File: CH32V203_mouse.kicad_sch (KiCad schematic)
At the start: 18 parts, among them J1 USB_C_Receptacle_USB2.0_16P_u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, U1 CH32V203G6U6, U2 USBLC6-2SC6, U3 XC6206P332MR, X1 16MHz

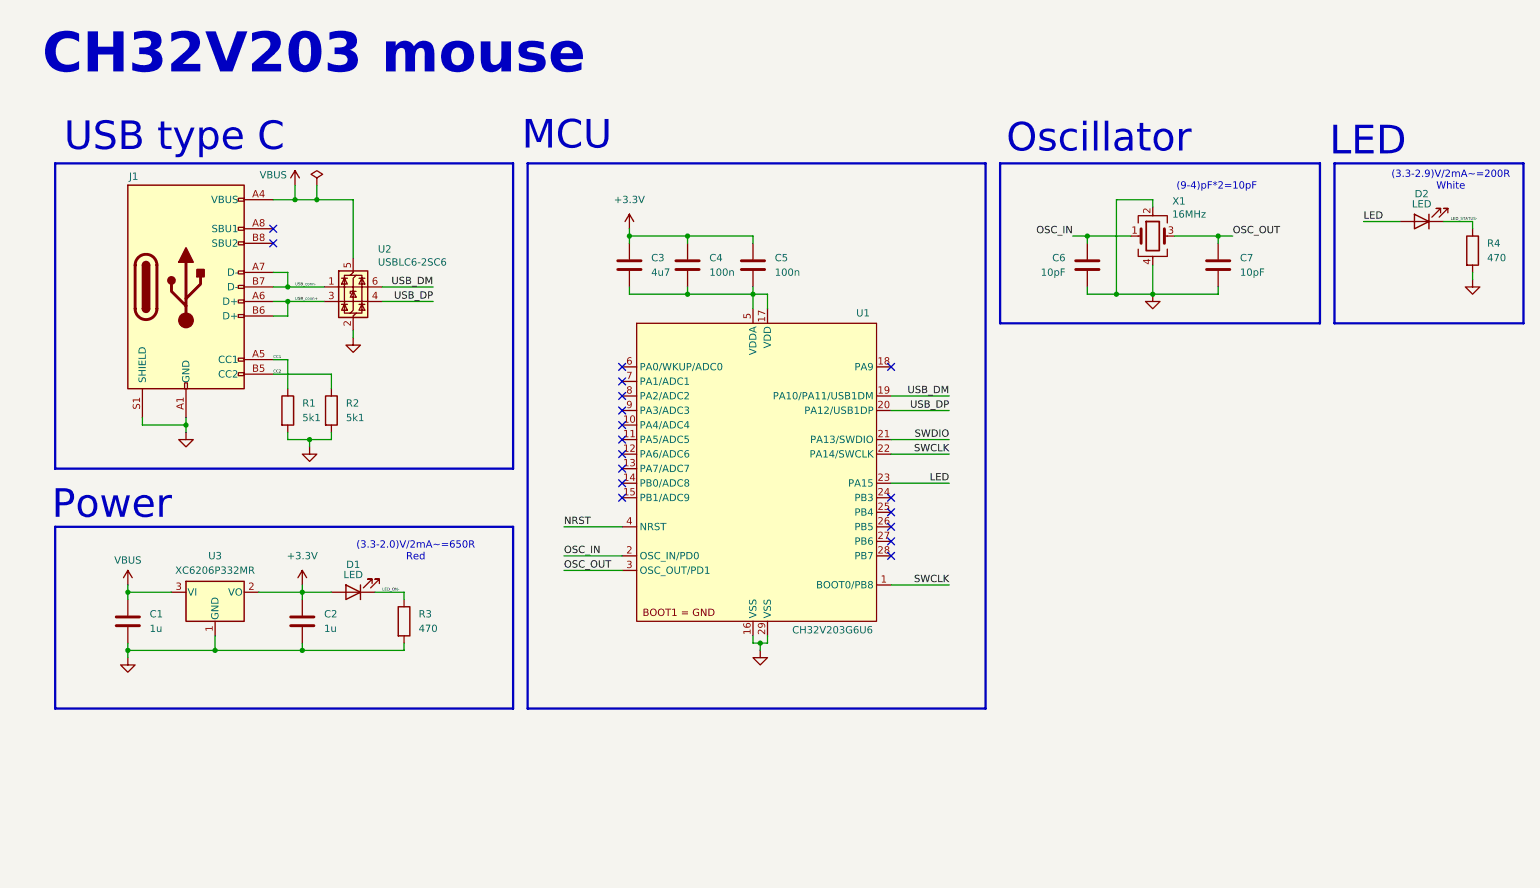
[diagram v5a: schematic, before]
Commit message: Switch circuit reset circuit debugging and UART connectors mounting holes
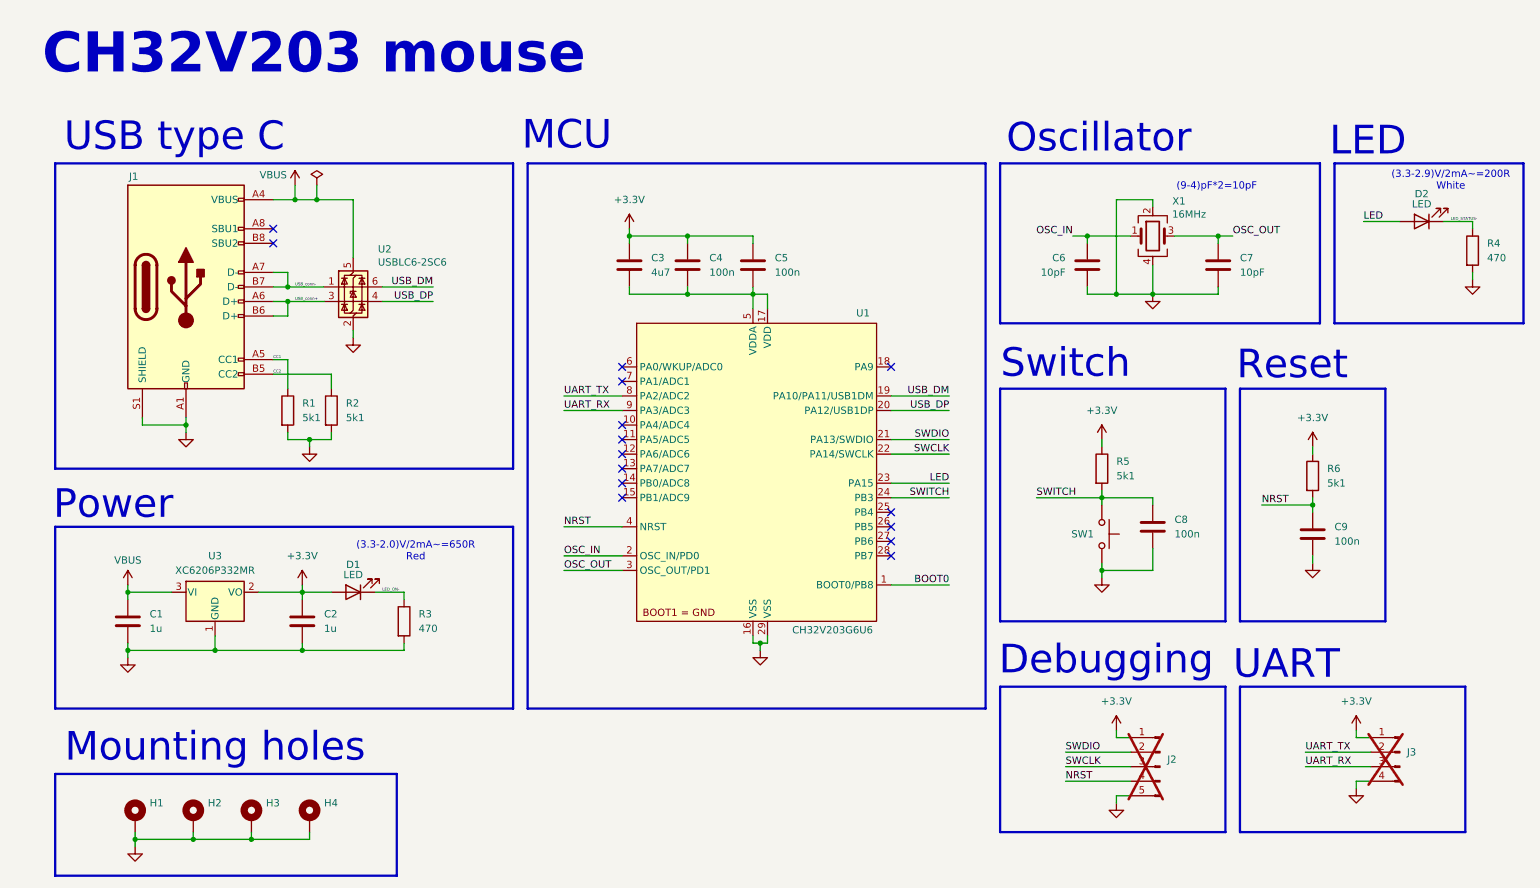
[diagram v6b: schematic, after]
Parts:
- added C8, C9: 100n, symbol Device:C
- added H1, H2, H3, H4: MountingHole_Pad, symbol Mechanical:MountingHole_Pad
- added J2: Conn_01x05_Pin, symbol Connector:Conn_01x05_Pin
- added J3: Conn_01x04_Pin, symbol Connector:Conn_01x04_Pin
- added R5, R6: 5k1, symbol Device:R
- added SW1: SW_Push, symbol Switch:SW_Push
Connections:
- net +3.3V: now also J2.1 (Pin_1), J3.1 (Pin_1), R5.1, R6.1
- net GND: now also C8.2, C9.2, H1.1, H2.1, H3.1, H4.1, J2.5 (Pin_5), J3.4 (Pin_4), SW1.2
- net NRST: now also C9.1, J2.4 (Pin_4), R6.2
- net SWCLK: now also J2.3 (Pin_3); no longer U1.1 (BOOT0/PB8)
- net SWDIO: now also J2.2 (Pin_2)
- net SWITCH: now reaches U1.24 (PB3)
- net SWITCH: now also C8.1, R5.2, SW1.1
- net UART_TX: now reaches U1.8 (PA2/ADC2)
- net UART_TX: now also J3.2 (Pin_2)
- net UART_RX: now reaches U1.9 (PA3/ADC3)
- net UART_RX: now also J3.3 (Pin_3)
- new net BOOT0: U1.1 (BOOT0/PB8)
- no-connect marks 18 -> 15
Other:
- note added: "Debugging"
- note added: "Mounting holes"
- note added: "Reset"
- note added: "Switch"
- note added: "UART"

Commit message: BOOT0 pull-down missing power flags
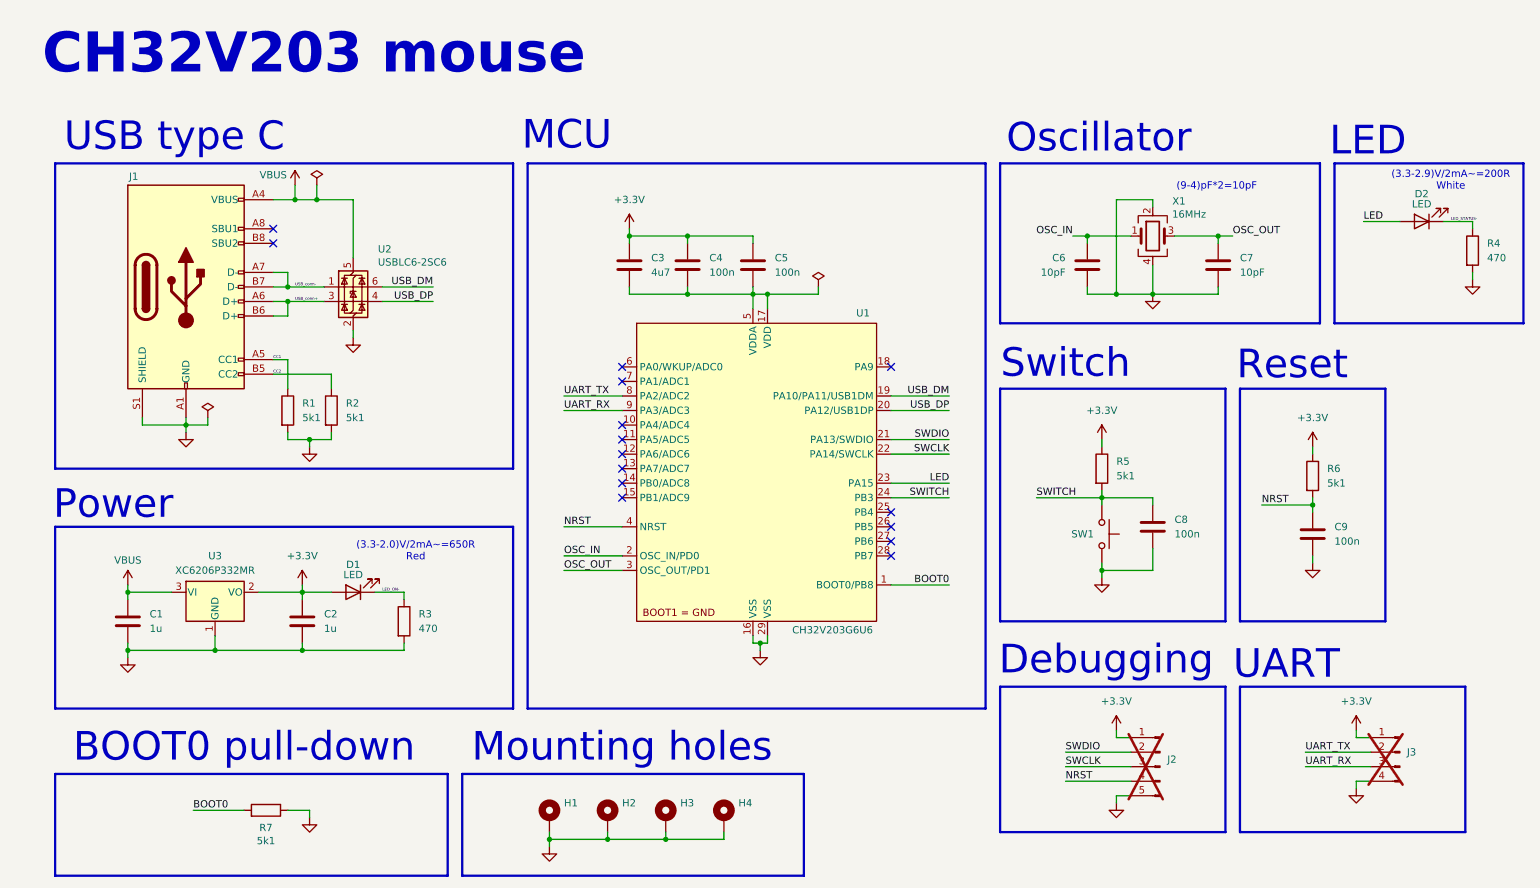
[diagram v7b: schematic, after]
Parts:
- added R7: 5k1, symbol Device:R
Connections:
- net BOOT0: now also R7.2
- net GND: now also R7.1
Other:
- note added: "BOOT0 pull-down"
- moved on the sheet: H1, H2, H3, H4

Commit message: Footprints selected
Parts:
- C1, C2, C3: footprint (none) -> Capacitor_SMD:C_0603_1608Metric_Pad1.08x0.95mm_HandSolder
- C4, C5, C6, C7, C8, C9, D1, D2: footprint (none) -> Capacitor_SMD:C_0402_1005Metric
- H1, H2, H3, H4: footprint (none) -> MountingHole:MountingHole_3.2mm_M3_DIN965_Pad
- J1: footprint (none) -> Connector_USB:USB_C_Receptacle_Palconn_UTC16-G
- J2: footprint (none) -> Connector_PinHeader_2.54mm:PinHeader_1x05_P2.54mm_Vertical
- J3: footprint (none) -> Connector_PinHeader_2.54mm:PinHeader_1x04_P2.54mm_Vertical
- R1, R2, R3, R4, R5, R6, R7: footprint (none) -> Resistor_SMD:R_0402_1005Metric
- SW1: footprint (none) -> Button_Switch_THT:SW_PUSH_6mm_H4.3mm
- X1: footprint (none) -> Crystal:Crystal_SMD_3225-4Pin_3.2x2.5mm
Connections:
- net VDD: now reaches C3.2, C4.2, C5.2, U1.17 (VDD), U1.5 (VDDA)
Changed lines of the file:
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@@
 		)
 	)
+	(label "VDD"
+		(at 146.05 64.77 0)
+		(fields_autoplaced yes)
+		(effects
+			(font
+				(size 0.5 0.5)
+			)
+			(justify left bottom)
+		)
+	)
 	(label "SWITCH"
 		(at 191.77 100.33 0)
@@
 			)
 		)
-		(property "Footprint" ""
+		(property "Footprint" "Resistor_SMD:R_0402_1005Metric"
 			(at 57.15 156.718 90)
 			(effects
@@
 			)
 		)
-		(property "Footprint" ""
+		(property "Footprint" "Capacitor_SMD:C_0402_1005Metric"
 			(at 131.7752 63.5 0)
 			(effects
@@
 			)
 		)
-		(property "Footprint" ""
+		(property "Footprint" "Capacitor_SMD:C_0402_1005Metric"
 			(at 72.39 116.84 0)
 			(effects
@@
 			)
 		)
-		(property "Footprint" ""
+		(property "Footprint" "Connector_PinHeader_2.54mm:PinHeader_1x04_P2.54mm_Vertical"
 			(at 255.27 144.78 0)
 			(effects
@@
 			)
 		)
-		(property "Footprint" ""
+		(property "Footprint" "Capacitor_SMD:C_0603_1608Metric_Pad1.08x0.95mm_HandSolder"
 			(at 64.4652 125.73 0)
 			(effects
@@
 			)
 		)
-		(property "Footprint" ""
+		(property "Footprint" "MountingHole:MountingHole_3.2mm_M3_DIN965_Pad"
 			(at 127 156.21 0)
 			(effects
@@
 			)
 		)
-		(property "Footprint" ""
+		(property "Footprint" "Resistor_SMD:R_0402_1005Metric"
 			(at 59.182 85.09 90)
 			(effects
@@
 			)
 		)
-		(property "Footprint" ""
+		(property "Footprint" "Capacitor_SMD:C_0603_1608Metric_Pad1.08x0.95mm_HandSolder"
 			(at 33.9852 125.73 0)
 			(effects
@@
 			)
 		)
-		(property "Footprint" ""
+		(property "Footprint" "MountingHole:MountingHole_3.2mm_M3_DIN965_Pad"
 			(at 137.16 156.21 0)
 			(effects
@@
 			)
 		)
-		(property "Footprint" ""
+		(property "Footprint" "Crystal:Crystal_SMD_3225-4Pin_3.2x2.5mm"
 			(at 212.09 54.61 0)
 			(effects
@@
 			)
 		)
-		(property "Footprint" ""
+		(property "Footprint" "Resistor_SMD:R_0402_1005Metric"
 			(at 266.192 57.15 90)
 			(effects
@@
 			)
 		)
-		(property "Footprint" ""
+		(property "Footprint" "Capacitor_SMD:C_0402_1005Metric"
 			(at 213.0552 109.22 0)
 			(effects
@@
 			)
 		)
-		(property "Footprint" ""
+		(property "Footprint" "Capacitor_SMD:C_0402_1005Metric"
 			(at 199.6948 63.5 0)
 			(effects
@@
 			)
 		)
-		(property "Footprint" ""
+		(property "Footprint" "Capacitor_SMD:C_0402_1005Metric"
 			(at 224.4852 63.5 0)
 			(effects
@@
 			)
 		)
-		(property "Footprint" ""
+		(property "Footprint" "Resistor_SMD:R_0402_1005Metric"
 			(at 66.802 85.09 90)
 			(effects
@@
 			)
 		)
-		(property "Footprint" ""
+		(property "Footprint" "Connector_PinHeader_2.54mm:PinHeader_1x05_P2.54mm_Vertical"
 			(at 213.36 147.32 0)
 			(effects
@@
 			)
 		)
-		(property "Footprint" ""
+		(property "Footprint" "Resistor_SMD:R_0402_1005Metric"
 			(at 238.252 96.52 90)
 			(effects
@@
 			)
 		)
-		(property "Footprint" ""
+		(property "Footprint" "Capacitor_SMD:C_0603_1608Metric_Pad1.08x0.95mm_HandSolder"
 			(at 121.6152 63.5 0)
 			(effects
@@
 			)
 		)
-		(property "Footprint" ""
+		(property "Footprint" "Resistor_SMD:R_0402_1005Metric"
 			(at 79.502 121.92 90)
 			(effects
@@
 			)
 		)
-		(property "Footprint" ""
+		(property "Footprint" "Resistor_SMD:R_0402_1005Metric"
 			(at 201.422 95.25 90)
 			(effects
@@
 			)
 		)
-		(property "Footprint" ""
+		(property "Footprint" "Button_Switch_THT:SW_PUSH_6mm_H4.3mm"
 			(at 208.28 106.68 0)
 			(effects
@@
 			)
 		)
-		(property "Footprint" ""
+		(property "Footprint" "MountingHole:MountingHole_3.2mm_M3_DIN965_Pad"
 			(at 106.68 156.21 0)
 			(effects
@@
 			)
 		)
-		(property "Footprint" ""
+		(property "Footprint" "Capacitor_SMD:C_0402_1005Metric"
 			(at 259.08 52.07 0)
 			(effects
@@
 			)
 		)
-		(property "Footprint" ""
+		(property "Footprint" "Capacitor_SMD:C_0402_1005Metric"
 			(at 143.2052 63.5 0)
 			(effects
@@
 			)
 		)
-		(property "Footprint" ""
+		(property "Footprint" "Connector_USB:USB_C_Receptacle_Palconn_UTC16-G"
 			(at 46.99 63.5 0)
 			(effects
@@
 			)
 		)
-		(property "Footprint" ""
+		(property "Footprint" "MountingHole:MountingHole_3.2mm_M3_DIN965_Pad"
 			(at 116.84 156.21 0)
 			(effects
@@
 			)
 		)
-		(property "Footprint" ""
+		(property "Footprint" "Capacitor_SMD:C_0402_1005Metric"
 			(at 240.9952 110.49 0)
 			(effects
